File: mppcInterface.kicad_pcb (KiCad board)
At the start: 2 copper layers, 65 x 56.5 mm, 93 parts, among them J1 Conn_Coaxial, J2 Conn_Coaxial, J3 Conn_Coaxial, J4 Conn_Coaxial, J5 Conn_Coaxial, J6 Conn_Coaxial, J7 Conn_Coaxial, J8 Conn_Coaxial, J9 Raspberry_Pi_2_3, U1 DAC60508ZRTE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

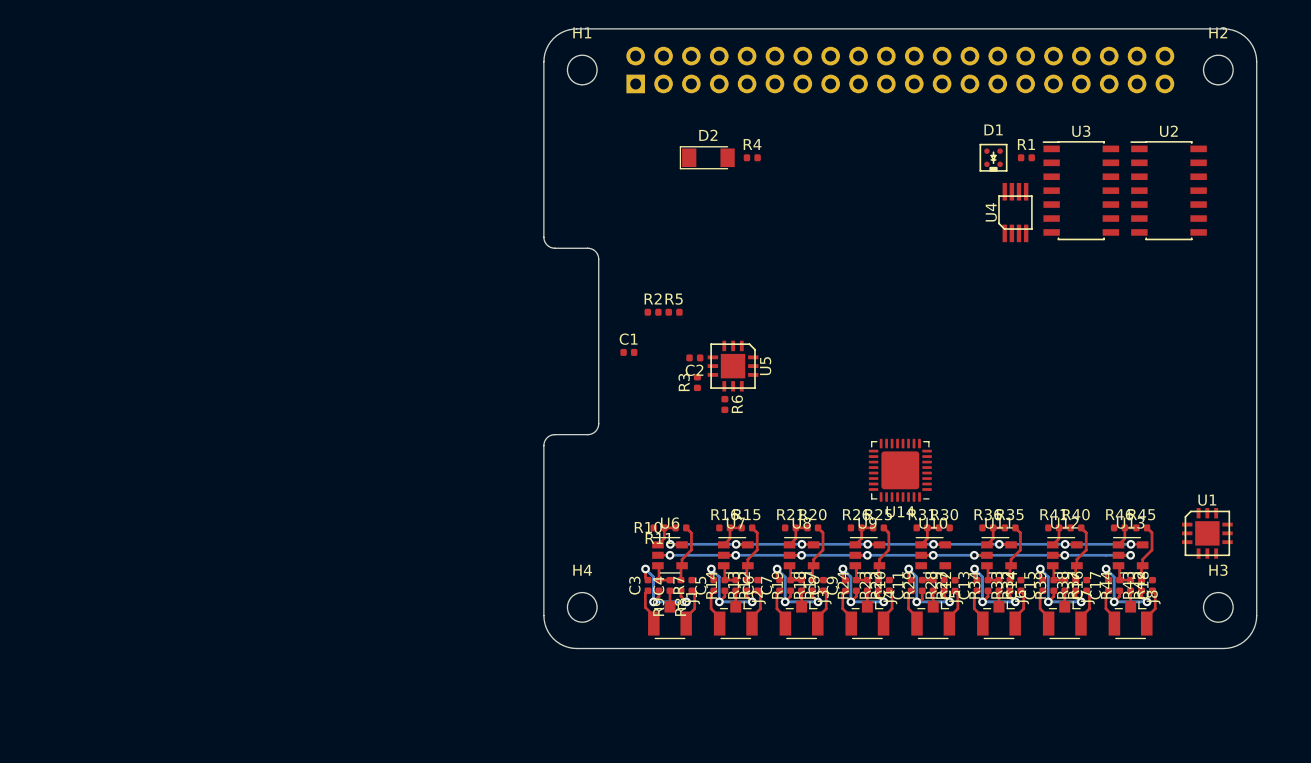
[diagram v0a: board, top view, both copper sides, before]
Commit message: Max1932 routed, fpga signal in router. Going to removed Voltage div here
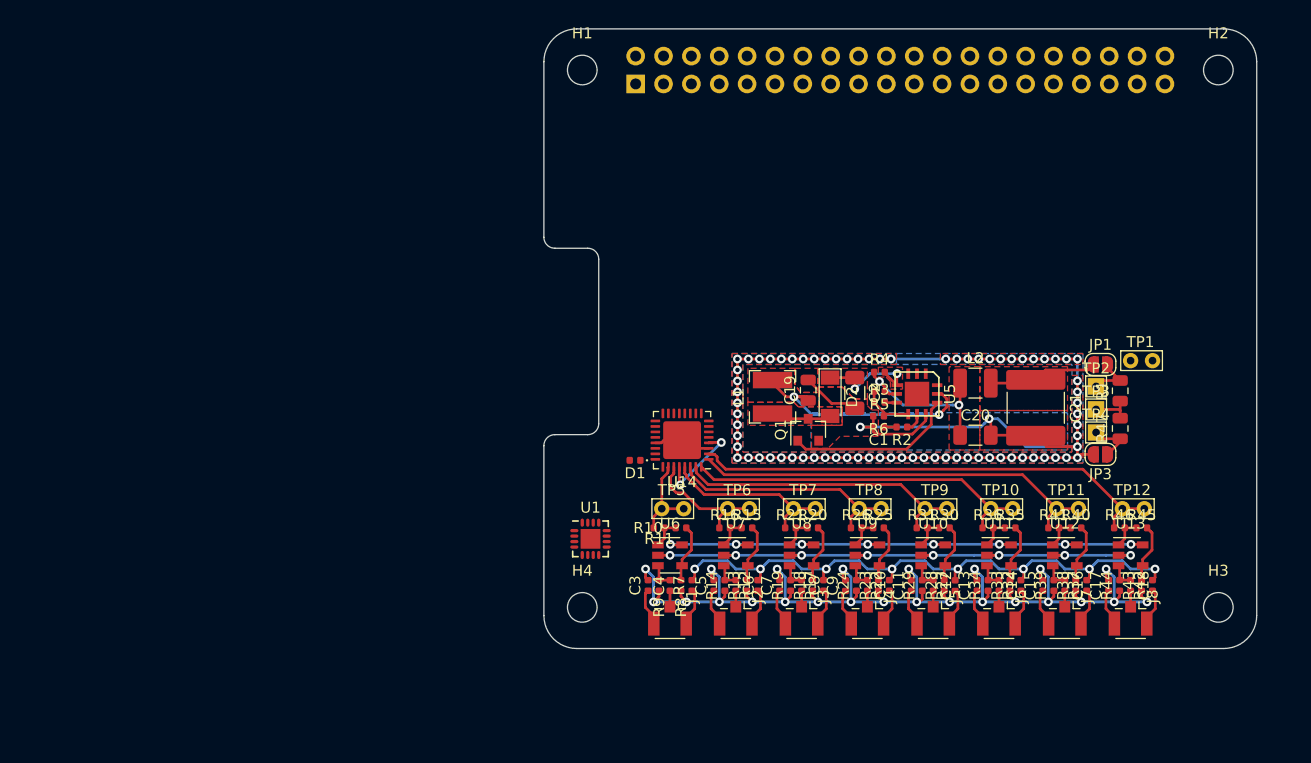
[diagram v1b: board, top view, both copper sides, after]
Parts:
- removed U2, U3: 74HC14, Package_SO:SOIC-14_3.9x8.7mm_P1.27mm
- removed U4: INA285, ina28x:TI-DGK-VSSOP-8
- added C19: 1u, Capacitor_SMD:C_0805_2012Metric, F.Cu at (-8.40, 4.70)
- added C20: 1u, Capacitor_SMD:C_1206_3216Metric, F.Cu at (6.85, 8.80)
- added C21: 10u, Capacitor_SMD:C_2220_5650Metric, F.Cu at (12.3, 6.30)
- added JP1: CAL, Jumper:SolderJumper-2_P1.3mm_Open_RoundedPad1.0x1.5mm, F.Cu at (18.2, 2.35)
- added JP3: CAL, Jumper:SolderJumper-2_P1.3mm_Open_RoundedPad1.0x1.5mm, F.Cu at (18.2, 10.6)
- added L1: 150uH, srn4018:SRN4018, F.Cu at (-11.7, 5.30)
- added L2: 1mH, Inductor_SMD:L_1210_3225Metric, F.Cu at (6.85, 4.05)
- added Q1: BSS123L, Package_TO_SOT_SMD:SOT-23, F.Cu at (-8.40, 8.30)
- added R47: 10K, Resistor_SMD:R_0805_2012Metric, F.Cu at (20.1, 8.19)
- added TP1: HV, TestPoint:TestPoint_Bridge_Pitch2.0mm_Drill0.7mm, F.Cu at (23.0, 2.00)
- added TP10: CH5, TestPoint:TestPoint_Bridge_Pitch2.0mm_Drill0.7mm, F.Cu at (10.2, 15.5)
- added TP11: CH6, TestPoint:TestPoint_Bridge_Pitch2.0mm_Drill0.7mm, F.Cu at (16.2, 15.5)
- added TP12: CH7, TestPoint:TestPoint_Bridge_Pitch2.0mm_Drill0.7mm, F.Cu at (22.2, 15.5)
- added TP2: DIV_A, TestPoint:TestPoint_THTPad_1.5x1.5mm_Drill0.7mm, F.Cu at (17.9, 4.35)
- added TP3: DIV_B, TestPoint:TestPoint_THTPad_1.5x1.5mm_Drill0.7mm, F.Cu at (17.9, 6.45)
- added TP4: DIV_C, TestPoint:TestPoint_THTPad_1.5x1.5mm_Drill0.7mm, F.Cu at (17.9, 8.55)
- added TP5: CH0, TestPoint:TestPoint_Bridge_Pitch2.0mm_Drill0.7mm, F.Cu at (-19.8, 15.5)
- added TP6: CH1, TestPoint:TestPoint_Bridge_Pitch2.0mm_Drill0.7mm, F.Cu at (-13.8, 15.5)
- added TP7: CH2, TestPoint:TestPoint_Bridge_Pitch2.0mm_Drill0.7mm, F.Cu at (-7.75, 15.5)
- added TP8: CH3, TestPoint:TestPoint_Bridge_Pitch2.0mm_Drill0.7mm, F.Cu at (-1.75, 15.5)
- added TP9: CH4, TestPoint:TestPoint_Bridge_Pitch2.0mm_Drill0.7mm, F.Cu at (4.25, 15.5)
- C2: footprint Capacitor_SMD:C_0402_1005Metric -> Capacitor_SMD:C_1206_3216Metric
- D1: value S13360-2050VE -> D; footprint s13360-2050ve:S13360-2050VE -> Diode_SMD:D_0402_1005Metric
- R1: value 4K99 -> 100K; footprint Resistor_SMD:R_0402_1005Metric -> Resistor_SMD:R_0805_2012Metric
- U1: footprint tqfn-12:TQFN-12 -> Package_DFN_QFN:QFN-16-1EP_3x3mm_P0.5mm_EP1.8x1.8mm
- moved U1 56.3 mm to (-28.2, 18.2)
- moved D1 42.8 mm to (-24.2, 11.1), turned to 180 degrees
- moved R2 25.0 mm to (0.14, 8.06), turned to 180 degrees
- moved D2 24.5 mm to (-6.40, 5.30), turned to 270 degrees
- moved C1 23.8 mm to (-1.98, 8.06), turned to 180 degrees
- moved R1 22.9 mm to (20.1, 4.75), turned to 90 degrees
- moved R4 22.7 mm to (-1.90, 3.05)
- moved U14 20.1 mm to (-19.9, 9.25)
- moved R5 20.1 mm to (-1.90, 4.80), turned to 180 degrees
- moved U5 17.0 mm to (1.52, 5.04)
- moved R3 16.7 mm to (-1.90, 5.80), turned to 0 degrees
- moved C2 14.9 mm to (-4.15, 4.95), turned to 270 degrees
- moved R6 14.1 mm to (-1.98, 7.06), turned to 180 degrees
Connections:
- D1 pad 1: (no net) -> Net-(D1-Pad1)
- D1 pad 2: (no net) -> +3V3
- R11 pad 1: /CH0-A -> CH0
- R16 pad 1: /CH1-A -> CH1
- R21 pad 1: /CH2-A -> CH2
- R26 pad 1: /CH3-A -> CH3
- R31 pad 1: /CH4-A -> CH4
- R36 pad 1: /CH5-A -> CH5
- R41 pad 1: /CH6-A -> CH6
- R46 pad 1: /CH7-A -> CH7
- U14 pad 1: Net-(U14-Pad1) -> CH6
- U14 pad 2: Net-(U14-Pad2) -> CH7
- U14 pad 24: Net-(U14-Pad24) -> Net-(D1-Pad1)
- U14 pad 26: Net-(U14-Pad26) -> CH0
- U14 pad 27: Net-(U14-Pad27) -> CH1
- U14 pad 29: Net-(U14-Pad29) -> CH2
- U14 pad 30: Net-(U14-Pad30) -> CH3
- U14 pad 31: Net-(U14-Pad31) -> CH4
- U14 pad 32: Net-(U14-Pad32) -> CH5
- U5 pad 11: GND -> VBUS
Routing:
- net GND: track 79.0 -> 232.2 mm, vias 24 -> 101
- net /HV: track 0.00 -> 65.3 mm, vias 0 -> 8
- net CH7: track 0.00 -> 44.0 mm
- net CH6: track 0.00 -> 37.6 mm
- net CH5: track 0.00 -> 32.0 mm
- net CH4: track 0.00 -> 26.8 mm
- net VBUS: track 0.00 -> 22.3 mm, vias 0 -> 2
- net CH3: track 0.00 -> 21.4 mm
- net Net-(C20-Pad1): track 0.00 -> 16.5 mm, vias 0 -> 2
- net CH2: track 0.00 -> 16.0 mm
- net Net-(Q1-Pad1): track 0.00 -> 15.7 mm
- net CH1: track 0.00 -> 12.0 mm
- net Net-(C2-Pad1): track 0.00 -> 10.4 mm, vias 0 -> 2
- net +3V3: track 0.00 -> 8.26 mm, vias 0 -> 2
- net CH0: track 0.00 -> 8.12 mm
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- added copper zone on F.Cu, net /HV
- added copper zone on B.Cu, net GND
- added copper zone on F.Cu, net GND
- added copper zone on F.Cu, net Net-(C2-Pad1)
- added copper zone on F.Cu, net Net-(C20-Pad1)
- added copper zone on F.Cu, net Net-(D2-Pad2)
- added copper zone on F.Cu, net VBUS
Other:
- board text added: "ADC"

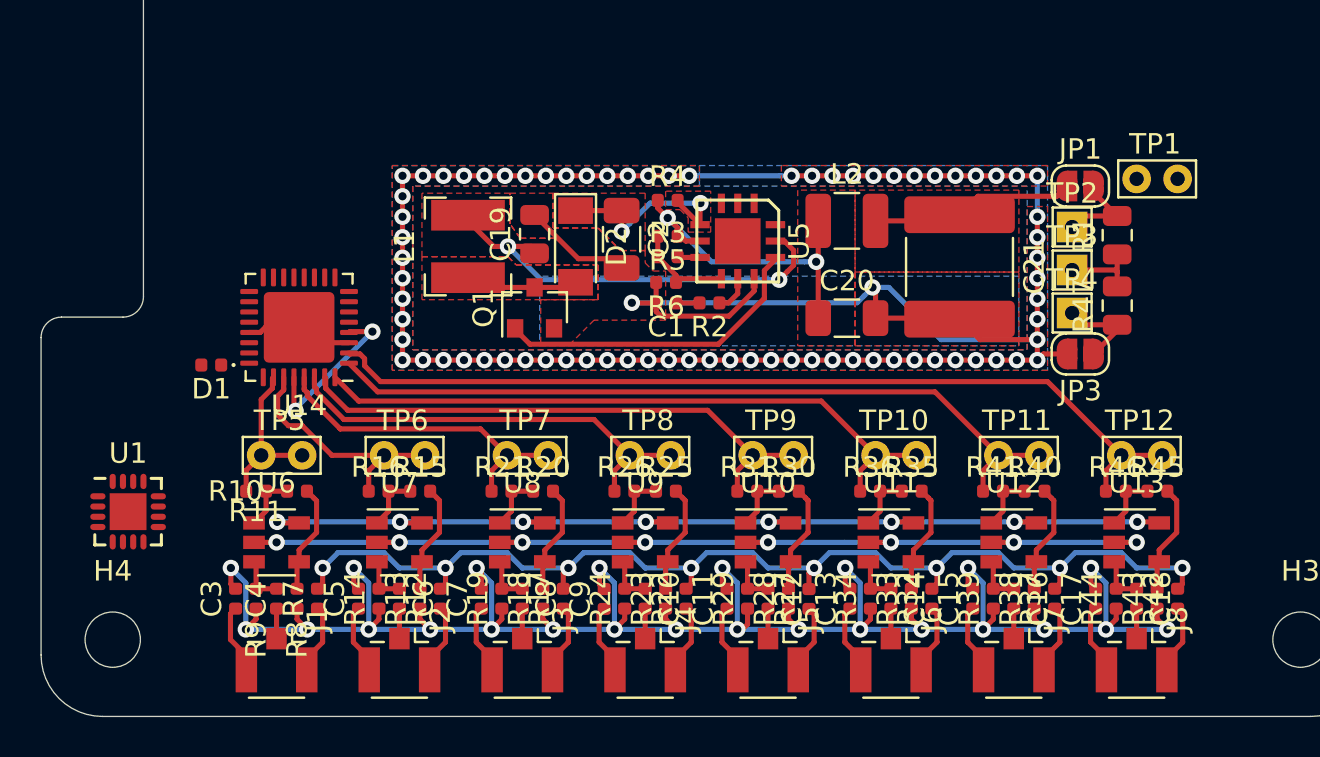
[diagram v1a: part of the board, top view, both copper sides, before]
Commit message: -5v supply, fpga routed
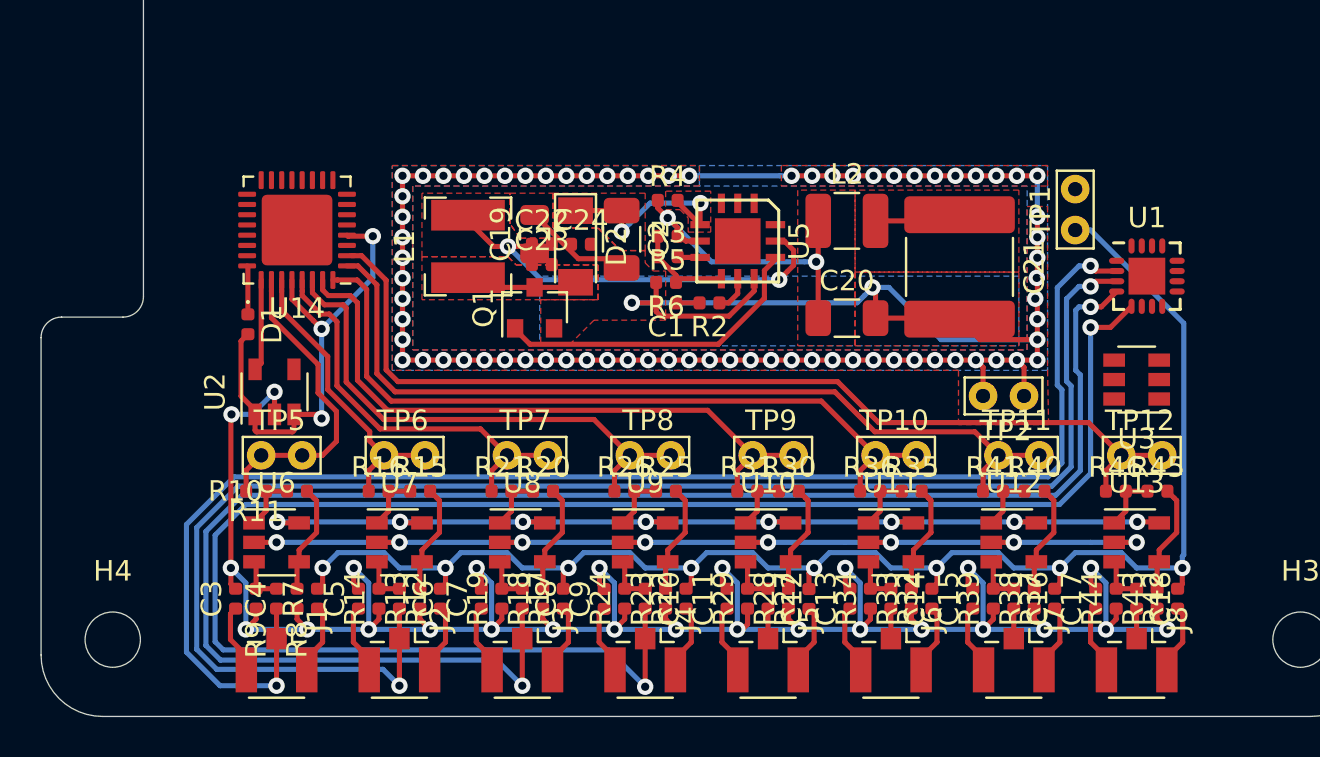
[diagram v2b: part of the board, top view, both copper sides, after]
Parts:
- removed JP1, JP3: CAL, Jumper:SolderJumper-2_P1.3mm_Open_RoundedPad1.0x1.5mm
- removed R1: 100K, Resistor_SMD:R_0805_2012Metric
- removed R47: 10K, Resistor_SMD:R_0805_2012Metric
- removed TP3: DIV_B, TestPoint:TestPoint_THTPad_1.5x1.5mm_Drill0.7mm
- removed TP4: DIV_C, TestPoint:TestPoint_THTPad_1.5x1.5mm_Drill0.7mm
- added C22: 10u, Capacitor_SMD:C_0402_1005Metric, F.Cu at (-8.04, 5.20)
- added C23: 1u, Capacitor_SMD:C_0402_1005Metric, F.Cu at (-8.04, 6.19)
- added C24: 10u, Capacitor_SMD:C_0402_1005Metric, F.Cu at (-6.13, 5.20)
- added U2: MIC5504-1.2YM5, Package_TO_SOT_SMD:SOT-23-5, F.Cu at (-21.1, 12.4)
- added U3: LM2776, Package_TO_SOT_SMD:SOT-23-6, F.Cu at (21.0, 11.8)
- TP2: value DIV_A -> GND; footprint TestPoint:TestPoint_THTPad_1.5x1.5mm_Drill0.7mm -> TestPoint:TestPoint_Bridge_Pitch2.0mm_Drill0.7mm
- moved U1 51.1 mm to (21.5, 6.75)
- moved TP2 9.33 mm to (13.5, 12.6)
- moved TP1 5.02 mm to (18.0, 2.50), turned to 270 degrees
- moved U14 4.75 mm to (-20.0, 4.50)
- moved D1 2.68 mm to (-22.4, 9.10), turned to 270 degrees
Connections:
- TP2 pad 1: Net-(JP1-Pad2) -> GND
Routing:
- net /DAC3: track 1.46 -> 84.5 mm, vias 0 -> 2
- net /DAC2: track 1.46 -> 79.8 mm, vias 0 -> 2
- net /DAC1: track 1.46 -> 75.4 mm, vias 0 -> 2
- net /DAC0: track 1.46 -> 71.2 mm, vias 0 -> 2
- net +3V3: track 8.26 -> 23.5 mm, vias 2 -> 3
- net /HV: track 65.3 -> 78.7 mm
- net GND: track 232.2 -> 240.4 mm, vias 101 -> 103
- net CH0: track 8.12 -> 15.2 mm
- net CH6: track 37.6 -> 42.2 mm
- net CH5: track 32.0 -> 36.6 mm
- net +1V2: track 0.00 -> 4.49 mm
- net Net-(JP1-Pad2): track 4.36 -> 0.00 mm
- net Net-(JP3-Pad1): track 4.34 -> 0.00 mm
- net CH4: track 26.8 -> 31.1 mm
- net CH7: track 44.0 -> 48.3 mm
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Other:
- board text removed: "ADC"

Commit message: routing only PI side left
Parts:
- moved C22 31.3 mm to (22.7, 10.9), turned to 270 degrees
- moved C24 29.8 mm to (22.7, 12.8), turned to 90 degrees
- moved C23 26.3 mm to (17.5, 12.3), turned to 270 degrees
- moved U3 0.90 mm to (20.1, 11.8)
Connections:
- C19 pad 1: VBUS -> +5V
- L1 pad 1: VBUS -> +5V
- U5 pad 11: VBUS -> +5V
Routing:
- net +5V: track 50.7 -> 94.1 mm, vias 8 -> 12
- net /DAC4: track 1.46 -> 42.5 mm, vias 0 -> 2
- net /DAC5: track 1.46 -> 37.7 mm, vias 0 -> 2
- net /DAC6: track 1.46 -> 33.6 mm, vias 0 -> 2
- net /DAC7: track 1.46 -> 29.5 mm, vias 0 -> 2
- net GND: track 240.4 -> 263.3 mm, vias 103 -> 105
- net VBUS: track 22.3 -> 0.00 mm, vias 2 -> 0
- net +3V3: track 23.5 -> 37.0 mm, vias 3 -> 5
- net -5V: track 50.8 -> 61.9 mm, vias 8 -> 9
- net /HV: track 78.7 -> 88.0 mm
- net Net-(C23-Pad2): track 0.00 -> 1.51 mm
- net Net-(C23-Pad1): track 0.00 -> 1.51 mm
- added copper zone on F.Cu, net +5V
- removed copper zone on F.Cu, net VBUS

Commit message: Wired up board
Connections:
- net Net-(J9-Pad10) renamed RXD
- net Net-(J9-Pad3) renamed SDA
- net Net-(J9-Pad5) renamed SDL
- net Net-(J9-Pad8) renamed TXD
- J9 pad 11: Net-(J9-Pad11) -> GPIO17
- J9 pad 12: Net-(J9-Pad12) -> GPIO18
- J9 pad 13: Net-(J9-Pad13) -> GPIO27
- J9 pad 15: Net-(J9-Pad15) -> FPGA_CS
- J9 pad 16: Net-(J9-Pad16) -> GPIO23
- J9 pad 18: Net-(J9-Pad18) -> FPGA_DONE
- J9 pad 22: Net-(J9-Pad22) -> FPGA_RST
- J9 pad 29: Net-(J9-Pad29) -> HV_CS
- J9 pad 37: Net-(J9-Pad37) -> DAC_CS
- J9 pad 7: Net-(J9-Pad7) -> CLK
- U14 pad 18: Net-(U14-Pad18) -> GPIO23
- U14 pad 19: Net-(U14-Pad19) -> GPIO27
- U14 pad 20: Net-(U14-Pad20) -> GPIO17
- U14 pad 22: Net-(U14-Pad22) -> GPIO18
- U14 pad 23: Net-(U14-Pad23) -> CLK
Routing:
- net +5V: track 94.1 -> 197.9 mm, vias 12 -> 17
- net GND: track 263.3 -> 360.0 mm
- net +3V3: track 37.0 -> 131.6 mm, vias 5 -> 8
- net SCLK: track 0.00 -> 94.0 mm, vias 0 -> 2
- net MOSI: track 0.00 -> 87.6 mm, vias 0 -> 2
- net MISO: track 0.00 -> 72.1 mm, vias 0 -> 1
- net GPIO18: track 0.00 -> 38.3 mm
- net FPGA_RST: track 0.00 -> 37.1 mm
- net GPIO23: track 0.00 -> 36.7 mm
- net CLK: track 0.00 -> 34.7 mm
- net GPIO17: track 0.00 -> 34.3 mm
- net GPIO27: track 0.00 -> 34.3 mm
- net FPGA_DONE: track 0.00 -> 34.2 mm, vias 0 -> 2
- net HV_CS: track 0.00 -> 31.6 mm, vias 0 -> 2
- net FPGA_CS: track 0.00 -> 31.5 mm
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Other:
- board text added: "GSU NPG sawaiz 2019"
- board text added: "MPPC Interface 1V1"
- board text added: "PROJ = coincidence BUILD = ./build DEVICE = 384 FOOTPRINT = qn32 FILES = top.v .PHONY: all clean burn all: mkdir -p $(BUILD) # synthesize using Yosys yosys -p "synth_ice40 -top top -blif $(BUILD)/$(PROJ).blif" $(FILES) # Place and route using arachne arachne-pnr -d $(DEVICE) -P $(FOOTPRINT) -o $(BUILD)/$(PROJ).asc -p pinmap.pcf $(BUILD)/$(PROJ).blif # Convert to bitstream using IcePack icepack $(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"
